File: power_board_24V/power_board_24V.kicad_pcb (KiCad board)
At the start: 2 copper layers, 100 x 60 mm, 56 parts, among them J1 Conn_01x02_Pin, J10 Conn_01x02_Socket, J11 Conn_01x02_Socket, J12 Conn_01x02_Socket, J13 Conn_01x02_Socket, J14 Conn_01x02_Socket, J15 Conn_01x04_Pin, J2 Conn_01x02_Pin, J3 Conn_01x02_Pin, J4 Conn_01x02_Pin, J5 Conn_01x02_Socket, J6 Conn_01x02_Socket, J7 Conn_01x02_Socket, J8 Conn_01x02_Socket, J9 Conn_01x02_Socket, K1 A31CCQ24VDC1D, Q1 2SA1015, Q2 BS170, U1 INA226

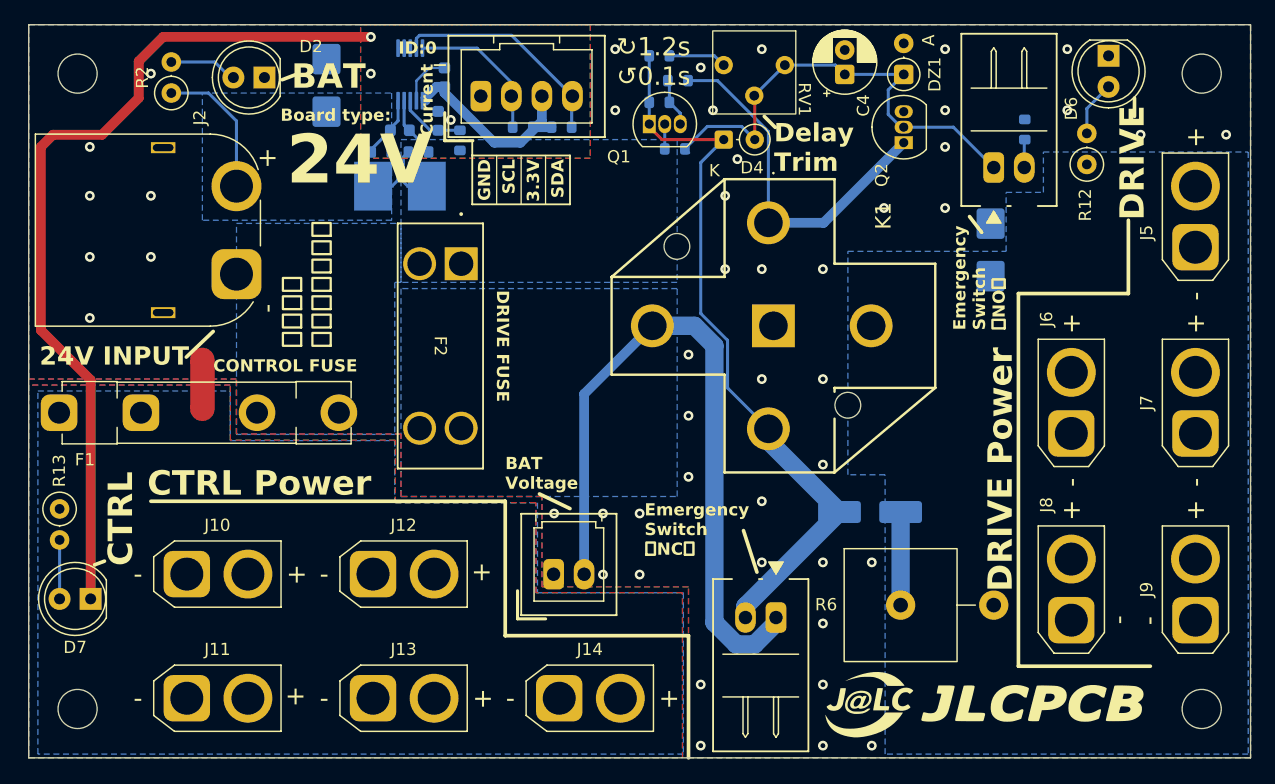
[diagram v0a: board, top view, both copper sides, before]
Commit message: 24V基板　Hiroseのコネクタにリファレンス番号を追加，基板IDを追加
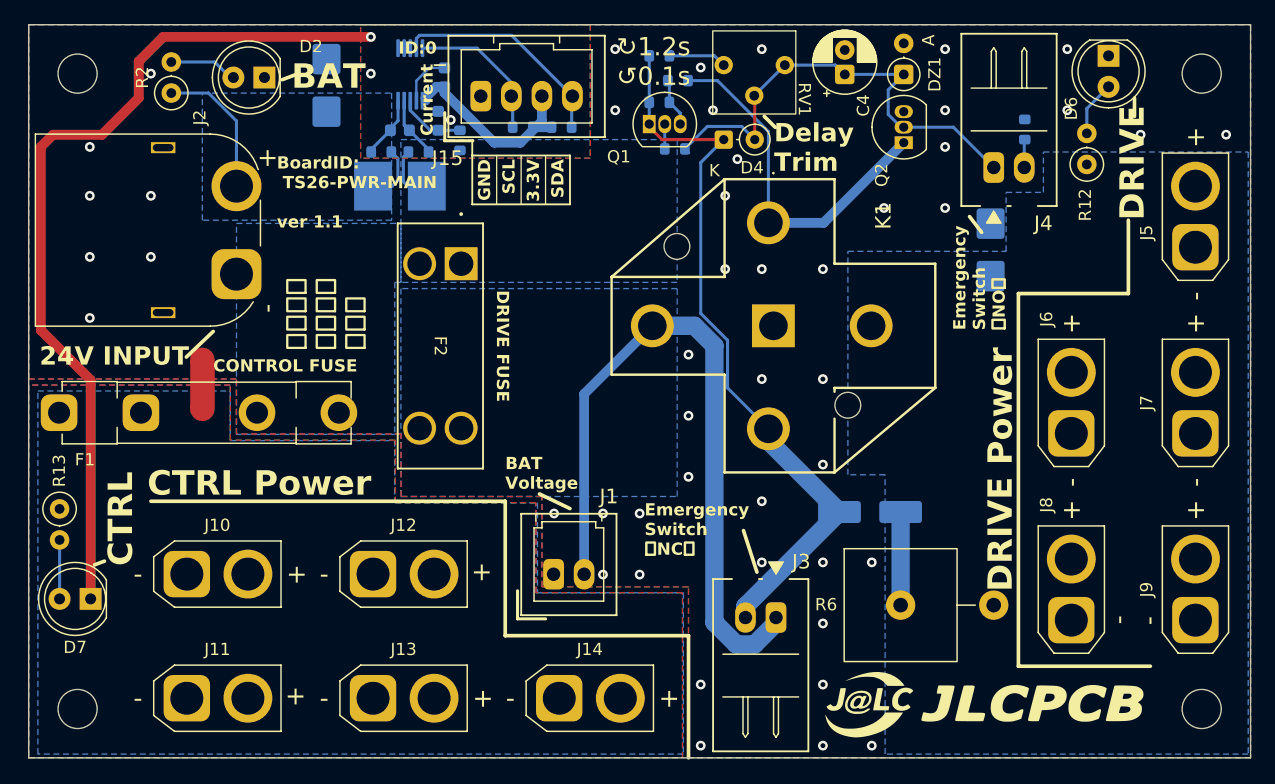
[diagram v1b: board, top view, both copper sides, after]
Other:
- board text added: "2026/09/19 Designed by E.Yoshioka"
- board text added: "BoardID: TS26-PWR-MAIN ver 1.1"
- board text added: "岡山大学 ロボット 研究会"
- board text removed: "2026/09/19 Designed by E.Yoshioka ver 1.0"
- board text removed: "24V"
- board text removed: "Board type:"
- board text removed: "岡山大学 ロボット研究会"
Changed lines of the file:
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@@
 		(tags "connector Hirose DF1E right-angle 2pin 2.5mm")
 		(property "Reference" "J3"
-			(at 1.25 -12.6 0)
+			(at -2.072 4.572 0)
 			(layer "F.SilkS")
-			(hide yes)
 			(effects
 				(font
@@
 		(sheetname "/")
 		(sheetfile "power_board_24V.kicad_sch")
-		(units
-			(unit
-				(name "A")
-				(pins "1" "2")
-			)
-		)
 		(duplicate_pad_numbers_are_jumpers no)
 		(fp_line
@@
 		(tags "connector Hirose DF1EC straight 2pin 2.5mm")
 		(property "Reference" "J1"
-			(at 1.25 -6.3 0)
+			(at 4.527 -6.363 0)
 			(layer "F.SilkS")
-			(hide yes)
 			(effects
 				(font
@@
 		(sheetname "/")
 		(sheetfile "power_board_24V.kicad_sch")
-		(units
-			(unit
-				(name "A")
-				(pins "1" "2")
-			)
-		)
 		(duplicate_pad_numbers_are_jumpers no)
 		(fp_line
@@
 		(tags "connector Hirose DF1EC straight 4pin 2.5mm")
 		(property "Reference" "J15"
-			(at 3.75 -6.3 0)
+			(at -2.724 5.08 0)
 			(layer "F.SilkS")
-			(hide yes)
 			(effects
 				(font
@@
 		(sheetname "/")
 		(sheetfile "power_board_24V.kicad_sch")
-		(units
-			(unit
-				(name "A")
-				(pins "1" "2" "3" "4")
-			)
-		)
 		(duplicate_pad_numbers_are_jumpers no)
 		(fp_line
@@
 		(tags "connector Hirose DF1E right-angle 2pin 2.5mm")
 		(property "Reference" "J4"
-			(at 1.25 -12.6 0)
+			(at 4.064 4.572 0)
 			(layer "F.SilkS")
-			(hide yes)
 			(effects
 				(font
@@
 		(sheetname "/")
 		(sheetfile "power_board_24V.kicad_sch")
-		(units
-			(unit
-				(name "A")
-				(pins "1" "2")
-			)
-		)
 		(duplicate_pad_numbers_are_jumpers no)
 		(fp_line
@@
 		(layer "Edge.Cuts")
 	)
-	(gr_text "Board type:"
-		(at 35.6 23.4 0)
+	(gr_text "BoardID:\n TS26-PWR-MAIN\n\nver 1.1"
+		(at 35.306 29.718 0)
 		(layer "F.SilkS")
 		(effects
@@
 		)
 	)
-	(gr_text "岡山大学\nロボット研究会"
-		(at 39.9 42.5 90)
+	(gr_text "岡山大学\nロボット\n研究会"
+		(at 42.672 42.672 90)
 		(layer "F.SilkS")
 		(effects
@@
 		)
 	)
-	(gr_text "24V"
-		(at 36.1 29.4 0)
-		(layer "F.SilkS" knockout)
-		(effects
-			(font
-				(face "Calibri")
-				(size 4 4)
-				(thickness 0.8)
-				(bold yes)
-			)
-			(justify left bottom)
-		)
-		(render_cache "24V" 0
-			(polygon
-				(pts
-					(xy 38.712177 28.429351) (xy 38.705338 28.563928) (xy 38.684822 28.655031) (xy 38.649162 28.705101)
-					(xy 38.600069 28.72) (xy 36.567236 28.72) (xy 36.463433 28.709253) (xy 36.392358 28.666999) (xy 36.352791 28.575896)
-					(xy 36.340579 28.420802) (xy 36.348639 28.267173) (xy 36.378681 28.153112) (xy 36.434856 28.05517)
-					(xy 36.523761 27.95039) (xy 37.135589 27.290935) (xy 37.307005 27.101504) (xy 37.430635 26.943377)
-					(xy 37.605512 26.657124) (xy 37.660027 26.528574) (xy 37.69173 26.418499) (xy 37.714933 26.211137)
-					(xy 37.686113 26.038213) (xy 37.650414 25.961453) (xy 37.60136 25.895819) (xy 37.539085 25.842001)
-					(xy 37.460676 25.800321) (xy 37.371492 25.774821) (xy 37.261374 25.765638) (xy 37.105594 25.776386)
-					(xy 36.975854 25.806427) (xy 36.757257 25.897285) (xy 36.599965 25.989364) (xy 36.53913 26.022892)
-					(xy 36.501779 26.031374) (xy 36.459281 26.01501) (xy 36.43046 25.960055) (xy 36.412875 25.856985)
-					(xy 36.406036 25.69896) (xy 36.410188 25.593203) (xy 36.4224 25.519197) (xy 36.444382 25.464242)
-					(xy 36.492009 25.407822) (xy 36.617794 25.326734) (xy 36.84323 25.232944) (xy 37.138276 25.156008)
-					(xy 37.30182 25.132678) (xy 37.474598 25.124745) (xy 37.740501 25.14323) (xy 37.956734 25.194354)
-					(xy 38.149184 25.279646) (xy 38.299651 25.388283) (xy 38.419051 25.524147) (xy 38.503349 25.683084)
-					(xy 38.553251 25.858513) (xy 38.570272 26.050181) (xy 38.562001 26.22125) (xy 38.537299 26.388946)
-					(xy 38.489039 26.556122) (xy 38.400767 26.748227) (xy 38.281846 26.942068) (xy 38.108408 27.174187)
-					(xy 37.901003 27.41359) (xy 37.608443 27.716406) (xy 37.195673 28.141632) (xy 38.589323 28.141632)
-					(xy 38.639637 28.157997) (xy 38.679448 28.208066) (xy 38.703872 28.297704)
-				)
-			)
-			(polygon
-				(pts
-					(xy 40.967271 25.178478) (xy 41.124319 25.200216) (xy 41.210537 25.236852) (xy 41.237892 25.288632)
-					(xy 41.237892 27.40695) (xy 41.552233 27.40695) (xy 41.589955 27.421378) (xy 41.627215 27.474605)
-					(xy 41.649222 27.553566) (xy 41.658722 27.69882) (xy 41.650365 27.830527) (xy 41.629902 27.912288)
-					(xy 41.593532 27.969459) (xy 41.552233 27.985317) (xy 41.237892 27.985317) (xy 41.237892 28.62621)
-					(xy 41.221528 28.674082) (xy 41.164131 28.708276) (xy 41.057397 28.728792) (xy 40.888136 28.735631)
-					(xy 40.722784 28.728792) (xy 40.61605 28.708276) (xy 40.561339 28.674082) (xy 40.546441 28.62621)
-					(xy 40.546441 27.985317) (xy 39.194068 27.985317) (xy 39.12568 27.975792) (xy 39.075122 27.931828)
-					(xy 39.04508 27.832909) (xy 39.035554 27.660963) (xy 39.039706 27.508555) (xy 39.05161 27.40695)
-					(xy 39.609281 27.40695) (xy 40.546441 27.40695) (xy 40.546441 25.796901) (xy 40.541067 25.796901)
-					(xy 39.609281 27.40695) (xy 39.05161 27.40695) (xy 39.053384 27.391807) (xy 39.080495 27.292889)
-					(xy 39.12568 27.19397) (xy 40.22404 25.266894) (xy 40.270446 25.22464) (xy 40.362037 25.194842)
-					(xy 40.511025 25.177257) (xy 40.729623 25.171639)
-				)
-			)
-			(polygon
-				(pts
-					(xy 43.91919 28.593726) (xy 43.883531 28.668953) (xy 43.812456 28.712428) (xy 43.678611 28.731479)
-					(xy 43.457571 28.735631) (xy 43.270237 28.734166) (xy 43.137857 28.727327) (xy 43.048953 28.711207)
-					(xy 42.991556 28.683852) (xy 42.95614 28.644284) (xy 42.932937 28.585422) (xy 41.880739 25.45545)
-					(xy 41.841172 25.299867) (xy 41.845091 25.248155) (xy 41.868527 25.213893) (xy 41.909958 25.192238)
-					(xy 41.984542 25.178478) (xy 42.214131 25.171639) (xy 42.41099 25.177257) (xy 42.520167 25.196308)
-					(xy 42.573412 25.237096) (xy 42.602233 25.30524) (xy 43.462944 28.028792) (xy 43.465631 28.028792)
-					(xy 44.309979 25.318918) (xy 44.337334 25.243935) (xy 44.393265 25.198995) (xy 44.506838 25.177257)
-					(xy 44.709071 25.171639) (xy 44.904221 25.179944) (xy 44.96654 25.19535) (xy 44.999965 25.219511)
-					(xy 45.016585 25.255184) (xy 45.016329 25.308171) (xy 44.974075 25.460823)
-				)
-			)
-		)
-	)
-	(gr_text "2026/09/19\nDesigned by E.Yoshioka\n\nver 1.0"
+	(gr_text "2026/09/19\nDesigned by E.Yoshioka"
 		(at 62.8 40.2 0)
 		(layer "B.SilkS")

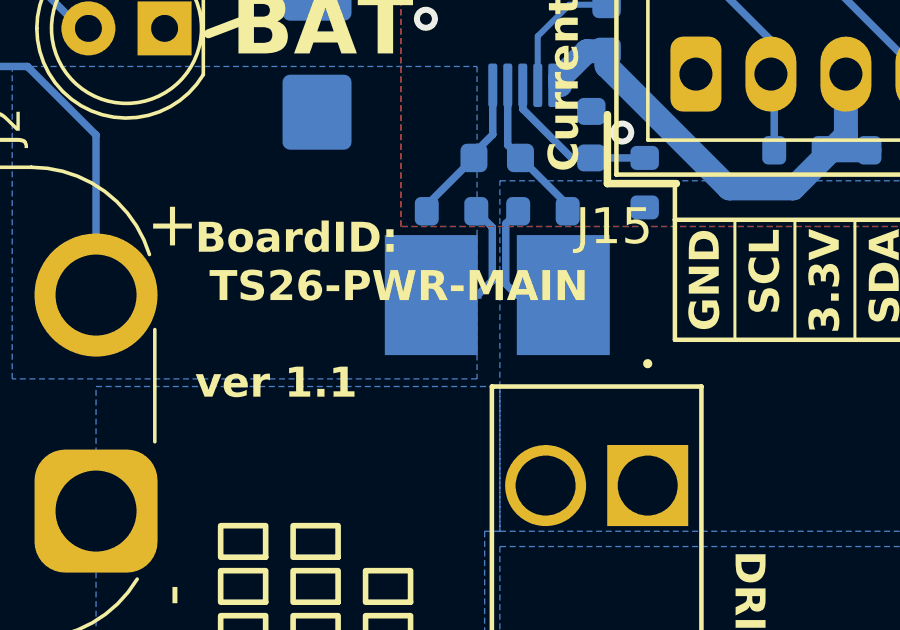
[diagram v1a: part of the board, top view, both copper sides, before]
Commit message: 24V基板　個体番号記入欄を追加，バージョンをver 0.2に変更 ver 1.nにしていたが，よく考えたら発注時に1.0にしたほうがいい．
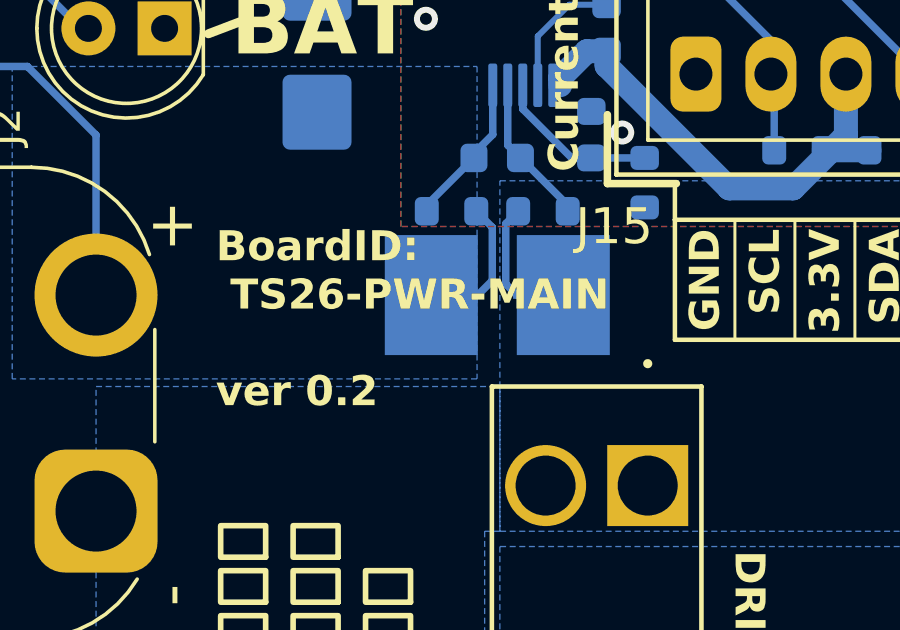
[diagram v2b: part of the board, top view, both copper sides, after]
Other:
- board text added: "BoardID: TS26-PWR-MAIN ver 0.2"
- board text added: "No."
- board text removed: "BoardID: TS26-PWR-MAIN ver 1.1"
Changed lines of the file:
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@@
+	)
+	(gr_rect
+		(start 28 50.45)
+		(end 40.5 57.35)
+		(stroke
+			(width 0.1)
+			(type solid)
+		)
+		(fill yes)
+		(layer "B.SilkS")
 	)
 	(gr_rect
@@
 		(layer "Edge.Cuts")
 	)
-	(gr_text "BoardID:\n TS26-PWR-MAIN\n\nver 1.1"
-		(at 35.306 29.718 0)
+	(gr_text "BoardID:\n TS26-PWR-MAIN\n\nver 0.2"
+		(at 36 30 0)
 		(layer "F.SilkS")
 		(effects
@@
 	)
 	(gr_text "2026/09/19\nDesigned by E.Yoshioka"
-		(at 62.8 40.2 0)
+		(at 61 40 0)
 		(layer "B.SilkS")
 		(effects
@@
 		)
 	)
+	(gr_text "No."
+		(at 45.7 57.2 0)
+		(layer "B.SilkS" knockout)
+		(effects
+			(font
+				(size 2 2)
+				(thickness 0.4)
+				(bold yes)
+			)
+			(justify left bottom mirror)
+		)
+	)

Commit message: 24V基板　JLCPCBロゴのサイズを変更，ver 0.3
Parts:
- removed the G*** at (93.2, 71.6)
- added G***: LOGO, OU_Picture:JLCPCB_Logo_5x23, F.Cu at (92.7, 71.6)
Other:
- board text added: "BoardID: TS26-PWR-MAIN ver 0.3"
- board text removed: "BoardID: TS26-PWR-MAIN ver 0.2"

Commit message: 24V基板　基板裏の日付を更新
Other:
- board text added: "2026/09/20 Designed by E.Yoshioka"
- board text removed: "2026/09/19 Designed by E.Yoshioka"
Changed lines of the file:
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@@
 		)
 	)
-	(gr_text "2026/09/19\nDesigned by E.Yoshioka"
+	(gr_text "2026/09/20\nDesigned by E.Yoshioka"
 		(at 61 40 0)
 		(layer "B.SilkS")
